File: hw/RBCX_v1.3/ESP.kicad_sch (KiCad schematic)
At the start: 13 parts

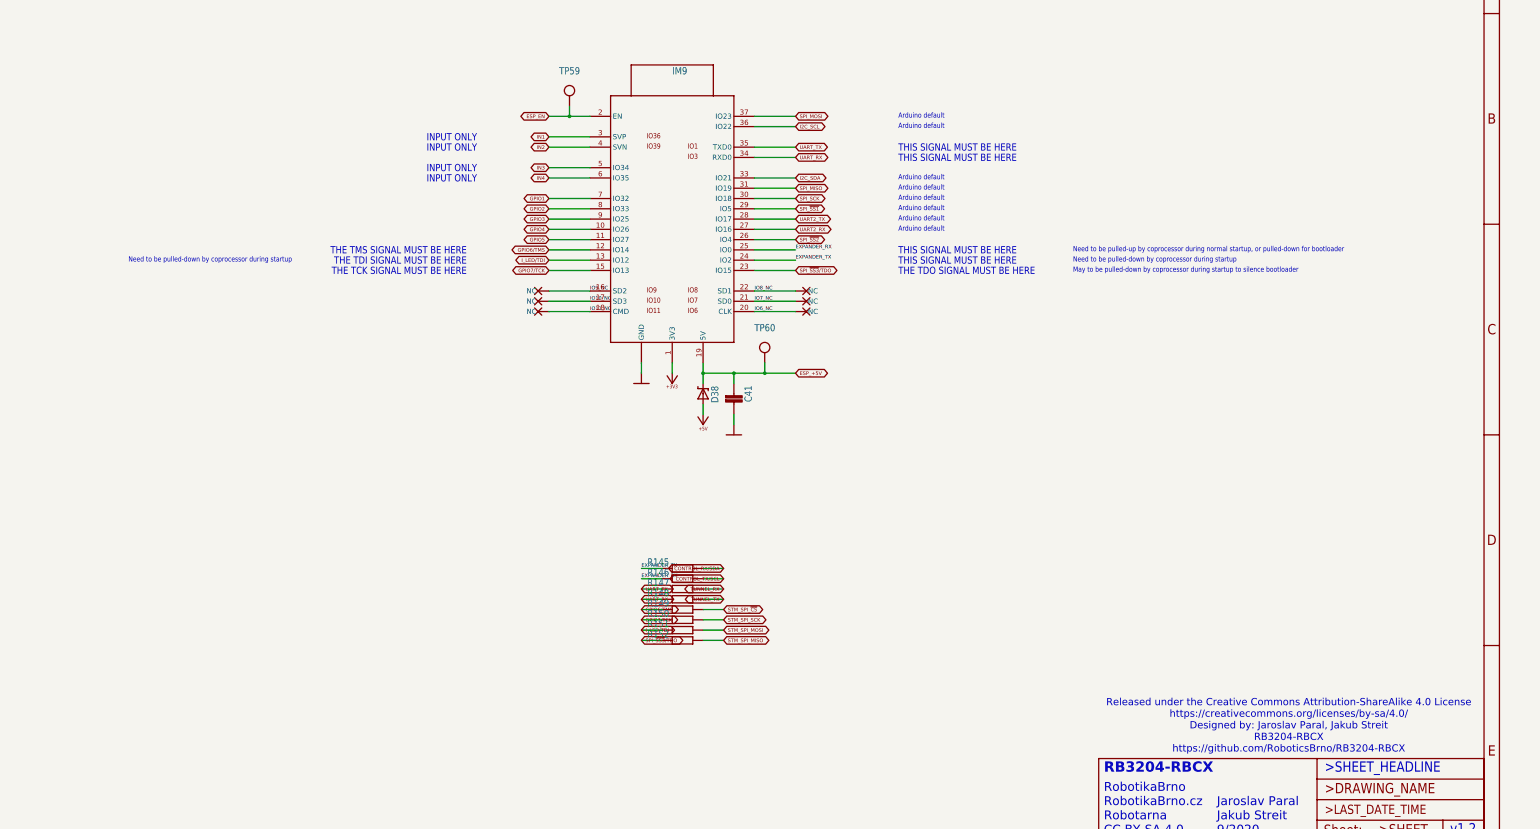
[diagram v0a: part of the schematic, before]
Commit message: Remove stepdowns, Micro-USB; fixup region names
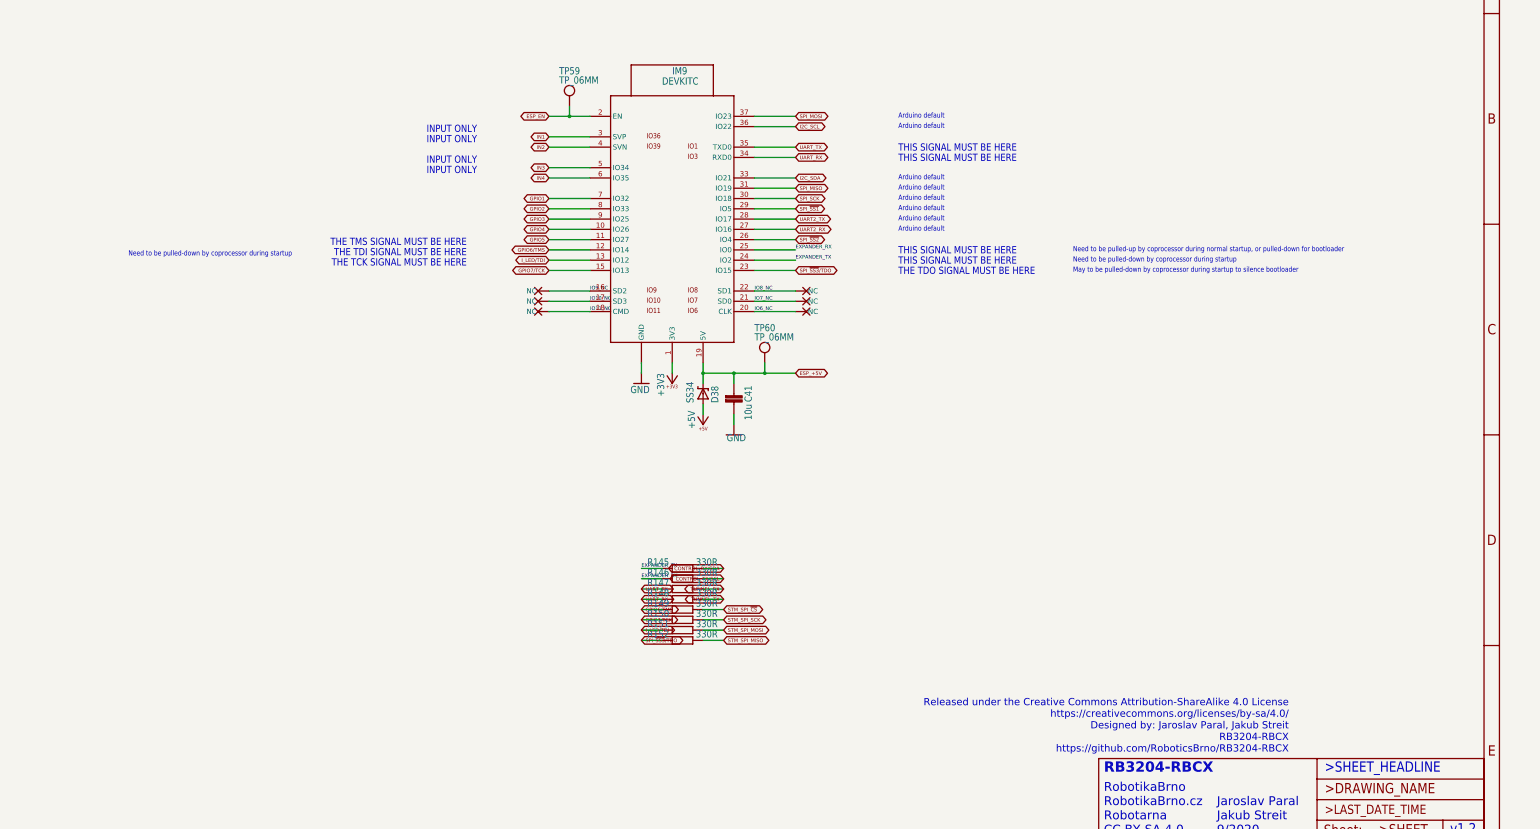
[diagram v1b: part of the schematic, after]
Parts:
- C41: footprint (none) -> RBCX:C0805
- D38: value (none) -> SS34; footprint (none) -> RBCX:SMA
- IM9: value (none) -> DEVKITC; footprint (none) -> RBCX:DEVKITC
- R145, R146, R147, R148, R149, R150, R151, R152: value (none) -> 330R; footprint (none) -> RBCX:R0402
- TP59, TP60: value (none) -> TP_06MM; footprint (none) -> RBCX:TP_06

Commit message: Everything everywhere all et once
Conversion to a new look
-  splitting the whole diagram for better orientation on multiple sheets using Kicad functions. Division of the whole schematics within several hierarchical sheets without globally named trac, using only wires, local labels and hierarchical labels.

Add new features
- Battery charger with cell balancer (With whole battery measurement)
- USB PD Sink Controller

Change old features
-  removing many 5V stepdowns and replacing them with only one strong stepdown (continuous 8A, peak 12A)
-  New power switcher design to connect VUSB to the VCC power line when no battery is connected.
(The reason for the new design is the implementation of Power deliveri => high voltage capability on VUSB 5-12V).

Remove micro_USB
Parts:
- removed C41: (no value), RBCX:C0805, symbol RBCX-eagle-import:C-EUC0805
- removed D38: SS34, RBCX:SMA, symbol RBCX-eagle-import:SHOTTKY-SMA
- removed IM9: DEVKITC, RBCX:DEVKITC, symbol RBCX-eagle-import:DEVKITC
- removed R145, R146, R147, R148, R149, R150, R151, R152: 330R, RBCX:R0402, symbol RBCX-eagle-import:R-EU_R0402
- removed TP59, TP60: TP_06MM, RBCX:TP_06, symbol RBCX-eagle-import:TP_06MM
- added C?: 10uF, Capacitor_SMD:C_0603_1608Metric, symbol Device:C
- added D?: D_Schottky, Diode_SMD:D_SOD-123F, symbol Device:D_Schottky
- added IM?: DEVKITC, RBCX:ESP32-DEVKITC, symbol RBCX-eagle-import:DEVKITC
- added J?: Conn_01x04, Connector_PinHeader_2.54mm:PinHeader_1x04_P2.54mm_Vertical, symbol Connector_Generic:Conn_01x04
- added J?: Conn_02x04_Counter_Clockwise, Connector_PinHeader_2.54mm:PinHeader_2x04_P2.54mm_Vertical, symbol Connector_Generic:Conn_02x04_Counter_Clockwise
- added LED? (x2): red, LED_SMD:LED_0603_1608Metric, symbol RBCX-eagle-import:LEDCHIPLED_0603
- added R? (x6): 330, Capacitor_SMD:C_0201_0603Metric, symbol Device:R
- added R? (x2): 1k, Resistor_SMD:R_0201_0603Metric, symbol Device:R
- added TP? (x2): TP_06MM, RBCX:TP_06MM, symbol RBCX-eagle-import:TP_06MM
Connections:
- net ESP_+5V: now also C?.1, D?.1 (K), IM?.19 (5V), TP?.P$1 (TP)
- net ESP_EN: now also IM?.2 (EN), TP?.P$1 (TP)
- net EXPANDER_RX: now also IM?.25 (IO0), R?.1
- net EXPANDER_TX: now also IM?.24 (IO2), R?.1
- net GND: now also C?.2, IM?.14 (GND), IM?.32 (GND), IM?.38 (GND), J?.2 (Pin_2), J?.5 (Pin_5), J?.6 (Pin_6), J?.7 (Pin_7), J?.8 (Pin_8), R?.1, R?.1
- net GPIO1: now also IM?.7 (IO32)
- net GPIO2: now also IM?.8 (IO33)
- net GPIO3: now also IM?.9 (IO25)
- net GPIO4: now also IM?.10 (IO26)
- net GPIO5: now also IM?.11 (IO27)
- net I2C_SCL: now also IM?.36 (IO22)
- net I2C_SDA: now also IM?.33 (IO21)
- net IN1: now also IM?.3 (SVP)
- net IN2: now also IM?.4 (SVN)
- net IN3: now also IM?.5 (IO34)
- net IN4: now also IM?.6 (IO35)
- net SPI_MISO: now also IM?.31 (IO19)
- net SPI_MOSI: now also IM?.37 (IO23)
- net SPI_SCK: now also IM?.30 (IO18)
- net SPI_~{SS1}: now also IM?.29 (IO5)
- net SPI_~{SS2}: now also IM?.26 (IO4)
- net TUNNEL_RX: now also R?.2
- net TUNNEL_TX: now also R?.2
- net UART2_RX: now also IM?.27 (IO16)
- net UART2_TX: now also IM?.28 (IO17)
- net UART_RX: now also IM?.34 (RXD0), R?.1, R?.1
- net UART_TX: now also IM?.35 (TXD0), R?.1, R?.1
- new net: LED?.C, R?.2 (x2)
- new net 3V3: IM?.1 (3V3), J?.1 (Pin_1), J?.1 (Pin_1), J?.2 (Pin_2), J?.3 (Pin_3), J?.4 (Pin_4), LED?.A, LED?.A
- new net 5V: D?.2 (A)
- new net CONTROL_RX/SDA: R?.2
- new net CONTROL_TX/SCL: R?.2
- new net ESP-UART-RX: J?.4 (Pin_4), R?.2
- new net ESP-UART-TX: J?.3 (Pin_3), R?.2
- new net GPIO6/TMS: IM?.12 (IO14)
- new net GPIO7/TCK: IM?.15 (IO13)
- new net I_LED/TDI: IM?.13 (IO12)
- new net SPI_~{SS3}/TDO: IM?.23 (IO15)
- no-connect marks 0 -> 6
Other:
- note added: "ESP UART"
- note added: "v1.3"
- note removed: "v1.2"

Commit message: Work in progress
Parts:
- removed J?: Conn_02x04_Counter_Clockwise, Connector_PinHeader_2.54mm:PinHeader_2x04_P2.54mm_Vertical, symbol Connector_Generic:Conn_02x04_Counter_Clockwise
- removed LED? (x2): red, LED_SMD:LED_0603_1608Metric, symbol RBCX-eagle-import:LEDCHIPLED_0603
- added D45, D46: red, LED_SMD:LED_0603_1608Metric, symbol Device:LED
- added J48: Conn_02x04_Odd_Even, Connector_PinHeader_2.54mm:PinHeader_2x04_P2.54mm_Vertical, symbol Connector_Generic:Conn_02x04_Odd_Even
- gave numbers to parts that had none: 14
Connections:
- net GND: now also J48.2 (Pin_2), J48.4 (Pin_4), J48.6 (Pin_6), J48.8 (Pin_8)
- net at R139.2: now also D46.1 (K)
- net at R138.2: now also D45.1 (K)
- net 3V3 renamed ESP-3V3
- net ESP-3V3: now also D45.2 (A), D46.2 (A), J48.1 (Pin_1), J48.3 (Pin_3), J48.5 (Pin_5), J48.7 (Pin_7)

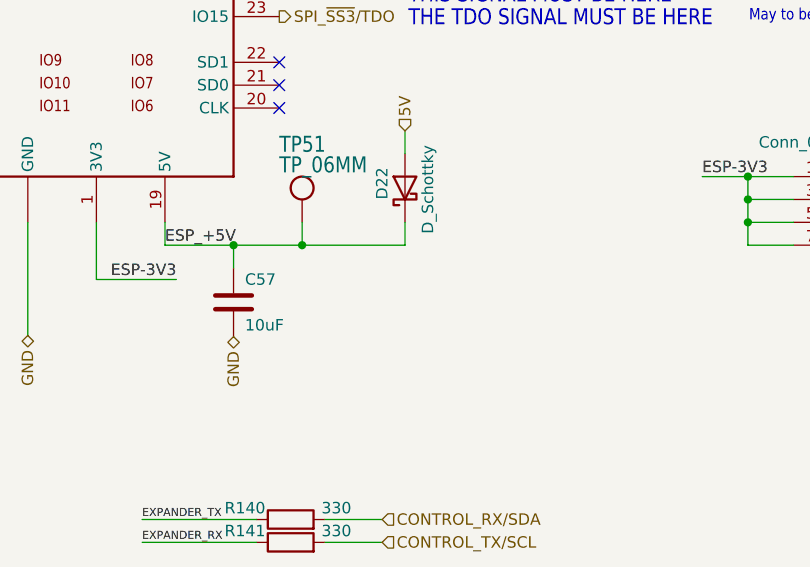
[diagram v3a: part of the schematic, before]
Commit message: New PCB layout
some changes of schema:
- change PD sink AO33772 to AO33771
- remove power switch
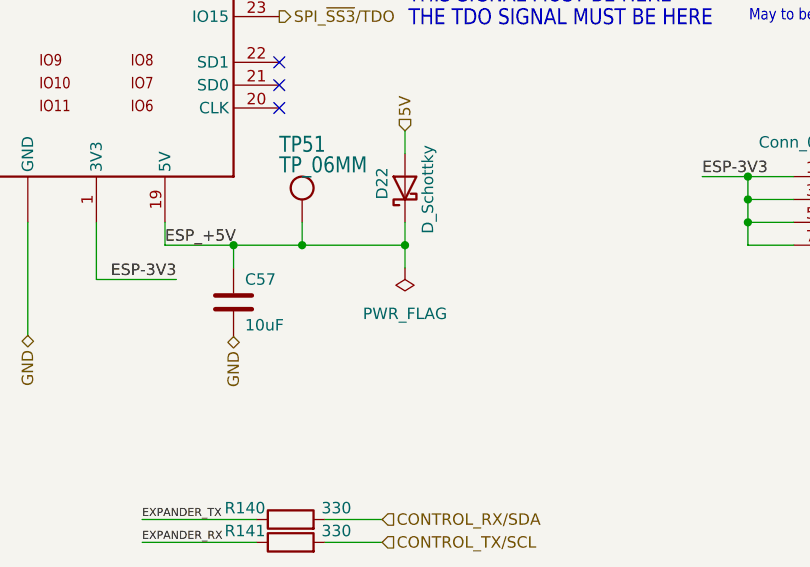
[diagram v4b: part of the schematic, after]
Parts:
- J47: footprint Connector_PinHeader_2.54mm:PinHeader_1x04_P2.54mm_Vertical -> RBCX:PinHeader_1x04_P2.54mm_Vertical
- J48: footprint Connector_PinHeader_2.54mm:PinHeader_2x04_P2.54mm_Vertical -> RBCX:PinHeader_2x04_P2.54mm_Vertical
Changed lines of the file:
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@@
   (junction (at 203.2 101.6) (diameter 0) (color 0 0 0 0)
+  )
+  (junction (at 165.1 109.22) (diameter 0) (color 0 0 0 0)
   )
   (junction (at 241.3 96.52) (diameter 0) (color 0 0 0 0)
@@
     (stroke (width 0) (type default) (color 0 0 0 0))
   )
+  (wire (pts (xy 165.1 109.22) (xy 165.1 111.76))
+    (stroke (width 0) (type default) (color 0 0 0 0))
+  )
   (wire (pts (xy 208.28 106.68) (xy 203.2 106.68))
     (stroke (width 0) (type default) (color 0 0 0 0))
@@
       (effects (font (size 1.27 1.27)) (justify left))
     )
-    (property "Footprint" "Connector_PinHeader_2.54mm:PinHeader_1x04_P2.54mm_Vertical" (id 2) (at 260.35 43.18 0)
+    (property "Footprint" "RBCX:PinHeader_1x04_P2.54mm_Vertical" (id 2) (at 260.35 43.18 0)
       (effects (font (size 1.27 1.27)) hide)
     )
@@
     (pin "P$1")
   )
+  (symbol (lib_id "power:PWR_FLAG") (at 165.1 111.76 180) (unit 1)
+    (in_bom yes) (on_board yes) (fields_autoplaced)
+    (property "Reference" "#FLG0103" (id 0) (at 165.1 113.665 0)
+      (effects (font (size 1.27 1.27)) hide)
+    )
+    (property "Value" "PWR_FLAG" (id 1) (at 165.1 116.84 0))
+    (property "Footprint" "" (id 2) (at 165.1 111.76 0)
+      (effects (font (size 1.27 1.27)) hide)
+    )
+    (property "Datasheet" "~" (id 3) (at 165.1 111.76 0)
+      (effects (font (size 1.27 1.27)) hide)
+    )
+    (pin "1")
+  )
   (symbol (lib_id "Device:R") (at 241.3 114.3 180) (unit 1)
     (in_bom yes) (on_board yes)
@@
       (effects (font (size 1.778 1.5113)) (justify left bottom))
     )
-    (property "Footprint" "RBCX:ESP32-DEVKITC" (id 2) (at 130.81 73.66 0)
+    (property "Footprint" "RBCX:ESP32-DEVKITC" (id 2) (at 130.81 73.66 90)
       (effects (font (size 1.27 1.27)) hide)
     )
@@
     (property "Reference" "J48" (id 0) (at 214.63 95.25 0))
     (property "Value" "Conn_02x04_Odd_Even" (id 1) (at 214.63 97.79 0))
-    (property "Footprint" "Connector_PinHeader_2.54mm:PinHeader_2x04_P2.54mm_Vertical" (id 2) (at 213.36 104.14 0)
-      (effects (font (size 1.27 1.27)) hide)
-    )
+    (property "Footprint" "RBCX:PinHeader_2x04_P2.54mm_Vertical" (id 2) (at 213.36 104.14 0)
+      (effects (font (size 1.27 1.27)) hide)
+    )

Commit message: Production files
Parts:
- IM3, TP50, TP51: JLCPCB_IGNORE (none) -> 1
- J47: JLCPCB_CORRECTION (none) -> 0;-3.81;90
- J48: JLCPCB_CORRECTION (none) -> 1.27;-3.81;90; LCSC C225289 -> C124386
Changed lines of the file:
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@@
+      (effects (font (size 1.27 1.27)) hide)
+    )
+    (property "JLCPCB_CORRECTION" "0;-3.81;90" (id 6) (at 260.35 43.18 0)
       (effects (font (size 1.27 1.27)) hide)
     )
@@
       (effects (font (size 1.27 1.27)) hide)
     )
+    (property "JLCPCB_IGNORE" "1" (id 4) (at 153.67 106.68 0)
+      (effects (font (size 1.27 1.27)) hide)
+    )
     (pin "P$1")
   )
@@
     )
     (property "Datasheet" "" (id 3) (at 130.81 73.66 0)
+      (effects (font (size 1.27 1.27)) hide)
+    )
+    (property "JLCPCB_IGNORE" "1" (id 4) (at 130.81 73.66 0)
       (effects (font (size 1.27 1.27)) hide)
     )
@@
       (effects (font (size 1.27 1.27)) hide)
     )
-    (property "LCSC" "C225289" (id 4) (at 213.36 104.14 0)
+    (property "LCSC" "C124386" (id 4) (at 213.36 104.14 0)
       (effects (font (size 1.27 1.27)) hide)
     )
     (property "Basic/Extended" "E" (id 5) (at 213.36 104.14 0)
+      (effects (font (size 1.27 1.27)) hide)
+    )
+    (property "JLCPCB_CORRECTION" "1.27;-3.81;90" (id 6) (at 213.36 104.14 0)
       (effects (font (size 1.27 1.27)) hide)
     )
@@
       (effects (font (size 1.27 1.27)) hide)
     )
+    (property "JLCPCB_IGNORE" "1" (id 4) (at 110.49 43.18 0)
+      (effects (font (size 1.27 1.27)) hide)
+    )
